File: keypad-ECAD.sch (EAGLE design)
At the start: 13 parts

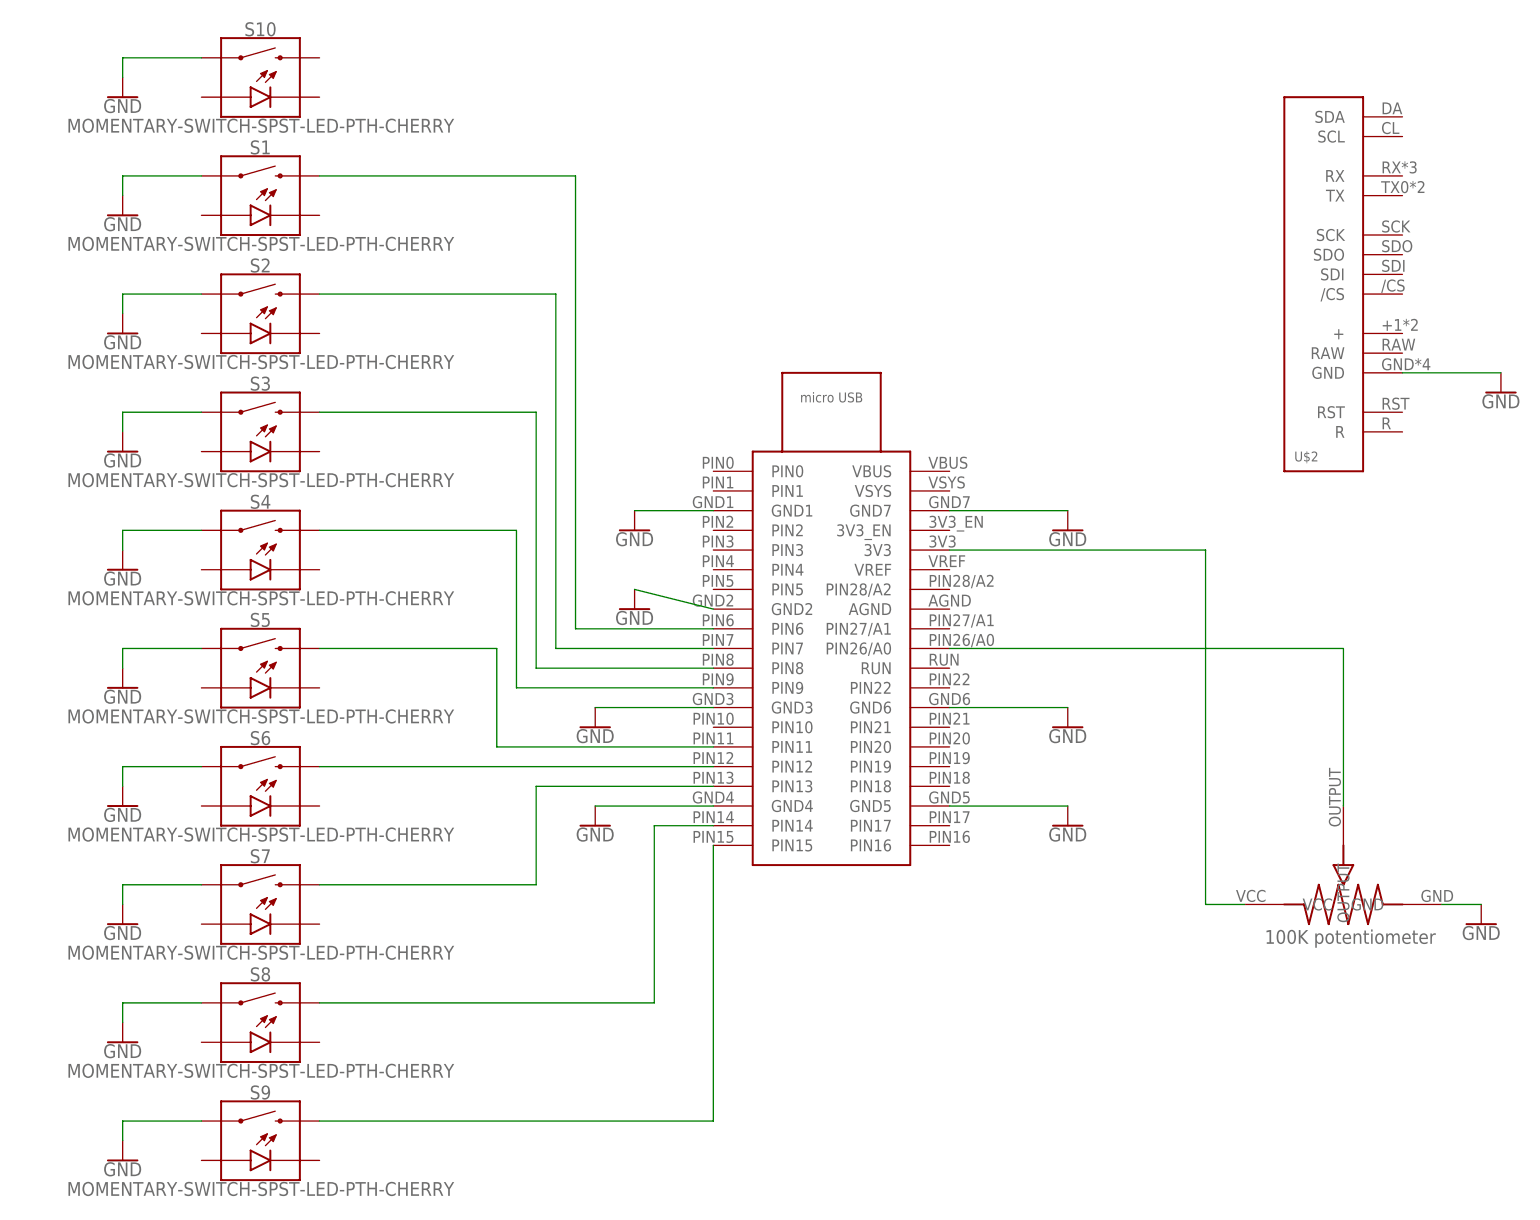
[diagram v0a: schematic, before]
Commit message: add OLED library and schematic connections
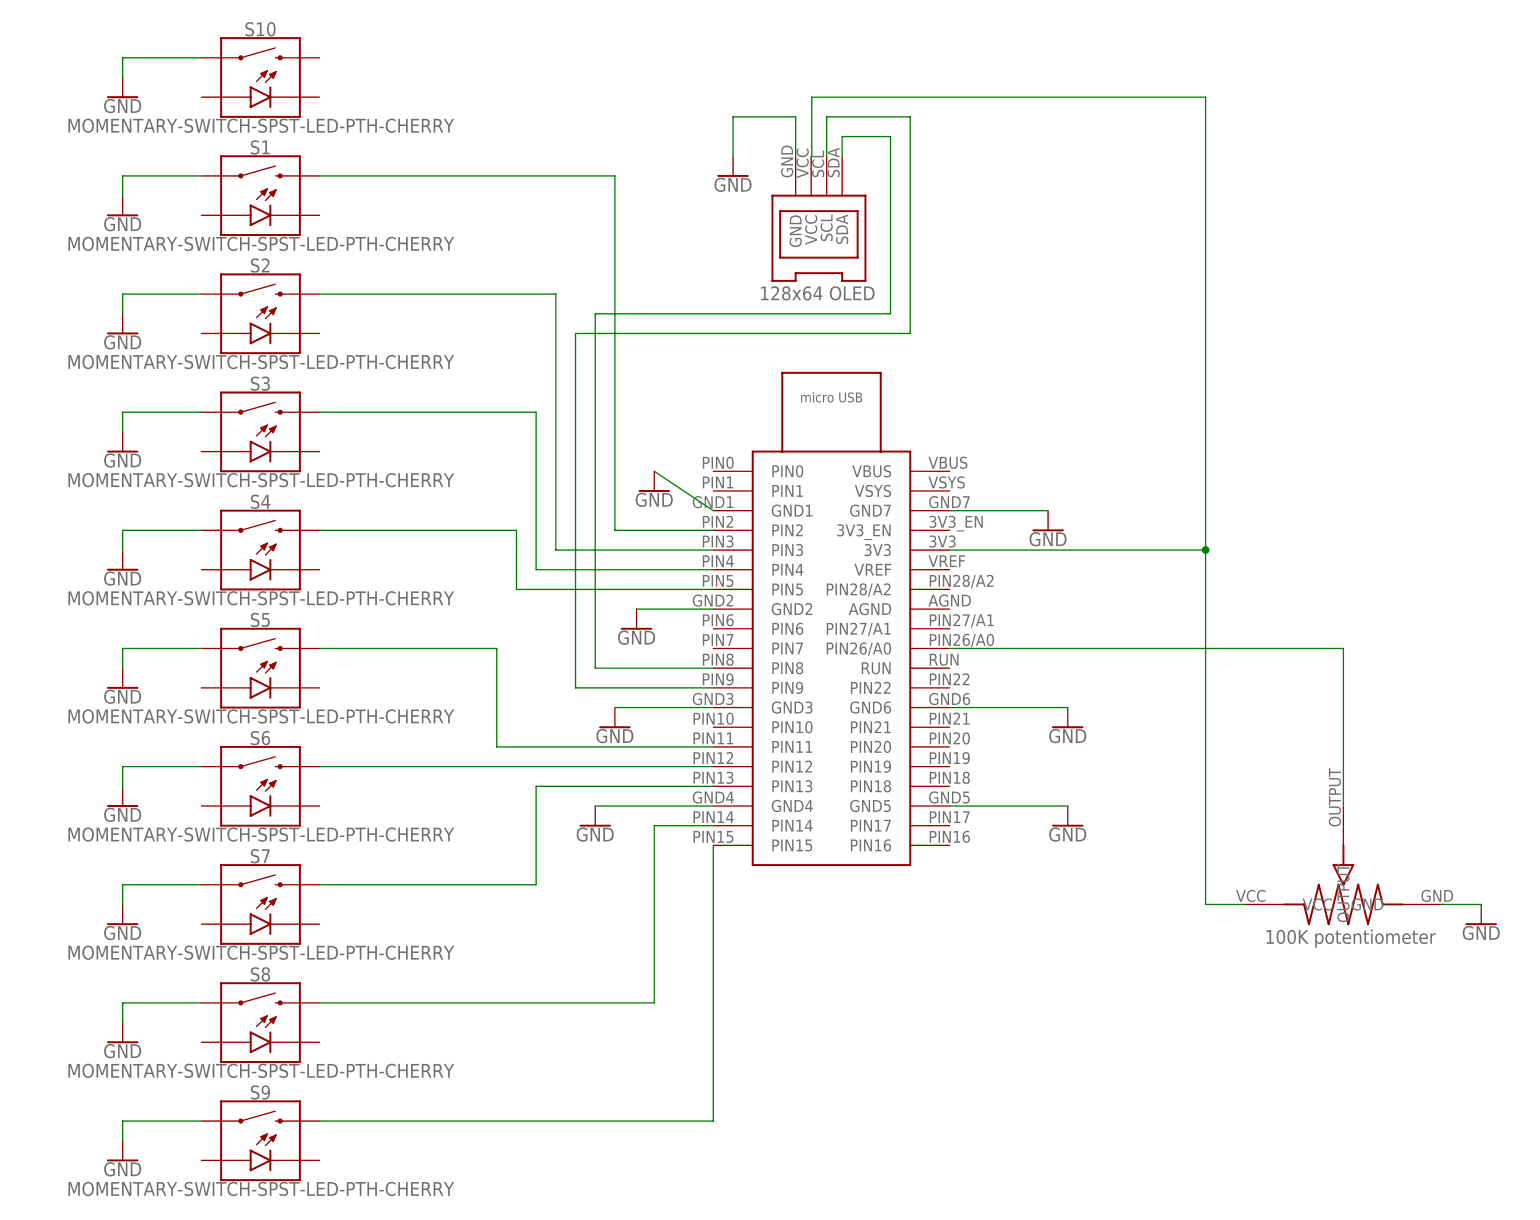
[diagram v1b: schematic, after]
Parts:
- U$2: value SPARKFUN_SERLCD_SERIAL -> 128X64-I2C-OLED; device SerLCD:SPARKFUN_SERLCD_SERIAL -> 128X64-I2C-OLED:128X64-I2C-OLED
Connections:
- new net N$12: S2.2, U$1.PIN3
- new net N$13: S1.2, U$1.PIN2
- net N$10: now also U$2.VCC
- net N$6: now also U$1.PIN8, U$2.SDA; no longer S4.2, U$1.PIN9
- net N$7: now also U$1.PIN9, U$2.SCL; no longer S3.2, U$1.PIN8
- net N$8: now also S4.2, U$1.PIN5; no longer S2.2, U$1.PIN7
- net N$9: now also S3.2, U$1.PIN4; no longer S1.2, U$1.PIN6

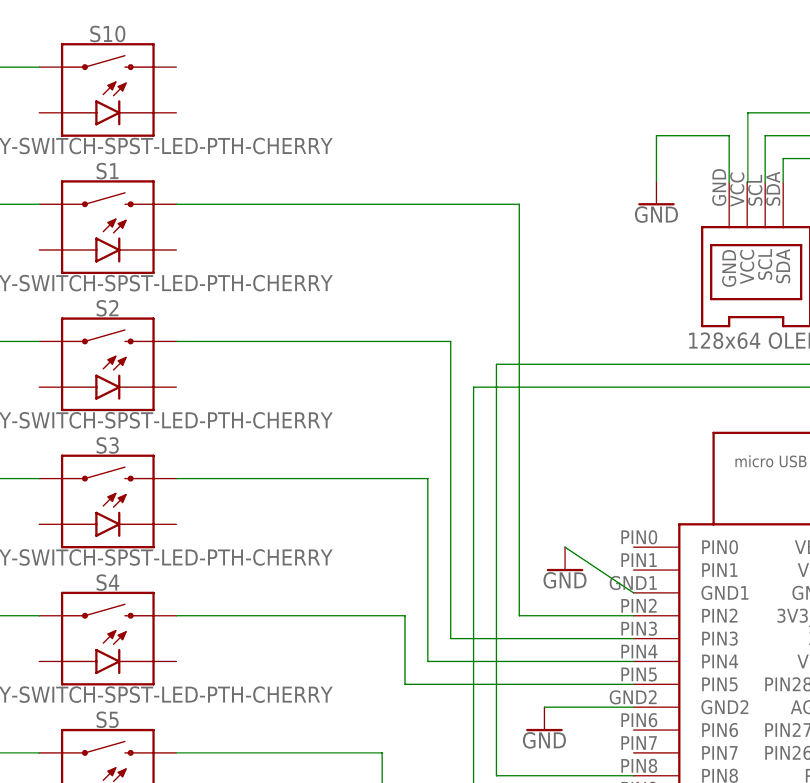
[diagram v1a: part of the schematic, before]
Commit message: fix missed button connection
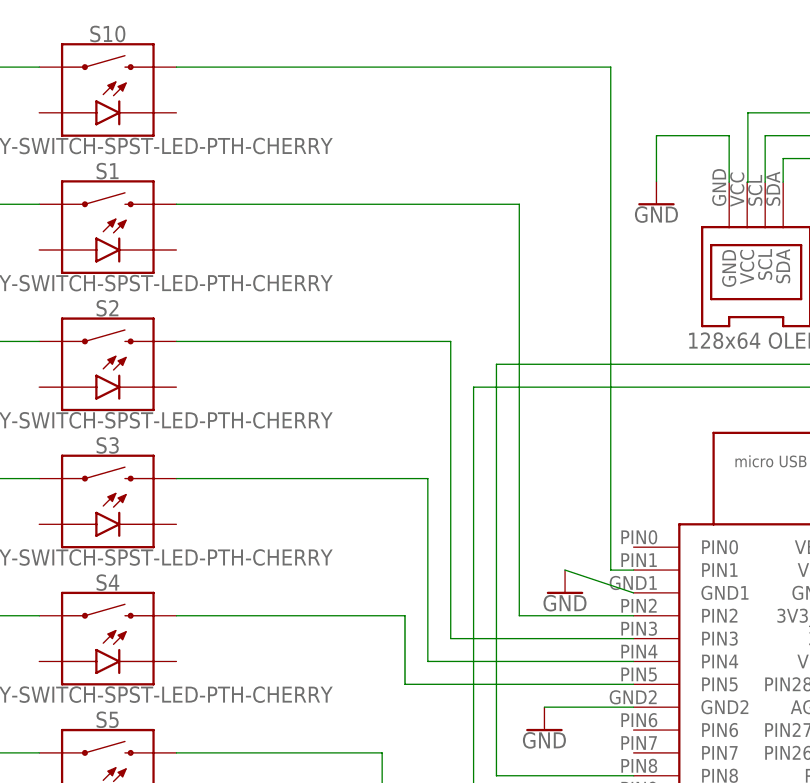
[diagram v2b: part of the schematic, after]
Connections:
- new net N$16: S10.2, U$1.PIN1
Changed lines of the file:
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@@
 <attribute name="VALUE" x="114.554" y="106.426" size="1.778" layer="96" align="top-center"/>
 </instance>
-<instance part="GND18" gate="1" x="116.84" y="124.46" smashed="yes">
-<attribute name="VALUE" x="116.84" y="124.206" size="1.778" layer="96" align="top-center"/>
+<instance part="GND18" gate="1" x="116.84" y="121.92" smashed="yes">
+<attribute name="VALUE" x="116.84" y="121.666" size="1.778" layer="96" align="top-center"/>
 </instance>
 <instance part="U$2" gate="G$1" x="132.08" y="162.56" smashed="yes"/>
@@
 <pinref part="U$1" gate="G$1" pin="GND1"/>
 <pinref part="GND18" gate="1" pin="GND"/>
-<wire x1="124.46" y1="121.92" x2="116.84" y2="127" width="0.1524" layer="91"/>
+<wire x1="124.46" y1="121.92" x2="116.84" y2="124.46" width="0.1524" layer="91"/>
 </segment>
 <segment>
@@
 </segment>
 </net>
+<net name="N$16" class="0">
+<segment>
+<pinref part="S10" gate="G$1" pin="2"/>
+<wire x1="73.66" y1="180.34" x2="121.92" y2="180.34" width="0.1524" layer="91"/>
+<wire x1="121.92" y1="180.34" x2="121.92" y2="124.46" width="0.1524" layer="91"/>
+<pinref part="U$1" gate="G$1" pin="PIN1"/>
+<wire x1="121.92" y1="124.46" x2="124.46" y2="124.46" width="0.1524" layer="91"/>
+</segment>
+</net>
